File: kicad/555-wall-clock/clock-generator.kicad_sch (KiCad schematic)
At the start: 3 parts, among them U1 LM555xN

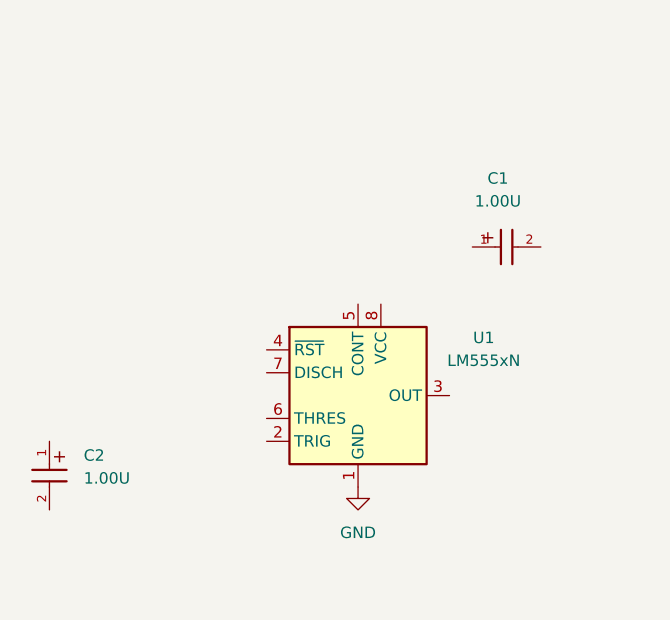
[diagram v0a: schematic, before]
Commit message: Wire in bypass caps
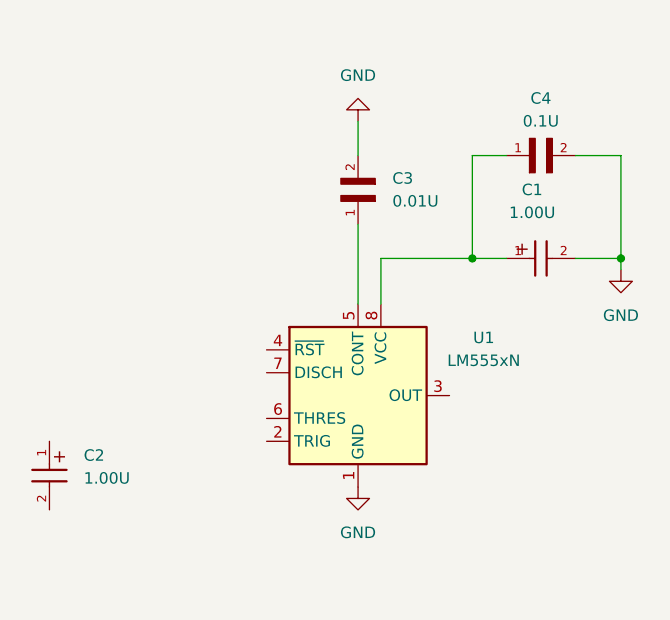
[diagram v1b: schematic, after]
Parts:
- added C3: 0.01U, B32529C0103J289:CAPRR500W50L730T250H650, symbol B3252*:B32529C0103J289
- added C4: 0.1U, B32529C0103J289:CAPRR500W50L730T250H650, symbol B3252*:B32529C0103J289
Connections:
- net GND: now also C1.2, C3.2, C4.2
- net at C1.1: now also U1.8 (VCC), C4.1
- net at U1.5 (CONT): now also C3.1
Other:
- moved on the sheet: C1

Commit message: Add 555 circuit RA/RB
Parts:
- added R1: 499k, symbol axial-130mil-body:res_ax_130mil
- added R2: 470k, symbol axial-130mil-body:res_ax_130mil
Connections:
- net GND: now also C2.2; no longer C1.2, C4.2
- net at U1.6 (THRES): now also C2.1, R2.2
- net at U1.7 (DISCH): now also R1.2, R2.1
- new net +BATT: C1.2, C4.2, R1.1
